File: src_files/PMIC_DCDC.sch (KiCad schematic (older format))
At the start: 49 parts

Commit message: littleupdate
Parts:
- C22, C23, C24, C25, C26, C27, C28, C29, C30, C31, C32, C33, C34, C35, C36, C37, C38, C39, C40, C41, C42, C43, C44, C45, C46, C47, C48, C49, C50, C51, C52, C53, C54, C55, C56, C57: renamed from C?; footprint (none) -> Capacitor_SMD:C_0402_1005Metric
- L1, L2, L3, L4, L5: renamed from L?; footprint (none) -> greencharge-footprints:SRP6540-5R6M
- R1, R2, R3, R4, R5, R6, R7: renamed from R?; footprint (none) -> Resistor_SMD:R_0402_1005Metric
- U2: renamed from U?; footprint (none) -> Package_DFN_QFN:TQFN-48-1EP_7x7mm_P0.5mm_EP5.1x5.1mm

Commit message: all screens added_3 items left
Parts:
- removed U2: RK809, Package_DFN_QFN:TQFN-48-1EP_7x7mm_P0.5mm_EP5.1x5.1mm, symbol GCL_Integrated-Circuits:RK809
- added U2: RK809, symbol GCL_Integrated-Circuits:RK809
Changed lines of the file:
@@
 $Descr A4 11693 8268
 encoding utf-8
-Sheet 3 11
+Sheet 3 12
 Title ""
 Date ""
@@
 Wire Wire Line
 	4875 1075 4550 1075
-$Comp
-L GCL_Integrated-Circuits:RK809 U?
-U 1 1 61D17743
-P 5875 925
-AR Path="/61D17743" Ref="U?"  Part="3"
-AR Path="/61CF51BC/61D17743" Ref="U2"  Part="1"
-F 0 "U2" H 5775 1075 50  0000 C CNN
-F 1 "RK809" H 5750 975 50  0000 C CNN
-F 2 "Package_DFN_QFN:TQFN-48-1EP_7x7mm_P0.5mm_EP5.1x5.1mm" H 5775 1125 50  0001 C CNN
-F 3 "" H 5775 1125 50  0001 C CNN
-	1    5875 925
-	1    0    0    -1
-$EndComp
 Text Label 3525 2275 0    50   ~ 0
 SW2
@@
 Wire Wire Line
 	6675 3825 6875 3825
+$Comp
+L GCL_Integrated-Circuits:RK809 U2
+U 3 1 625FB264
+P 5875 925
+F 0 "U2" H 5775 1090 50  0000 C CNN
+F 1 "RK809" H 5775 999 50  0000 C CNN
+F 2 "" H 5775 1125 50  0001 C CNN
+F 3 "" H 5775 1125 50  0001 C CNN
+	3    5875 925
+	1    0    0    -1
+$EndComp
 $EndSCHEMATC

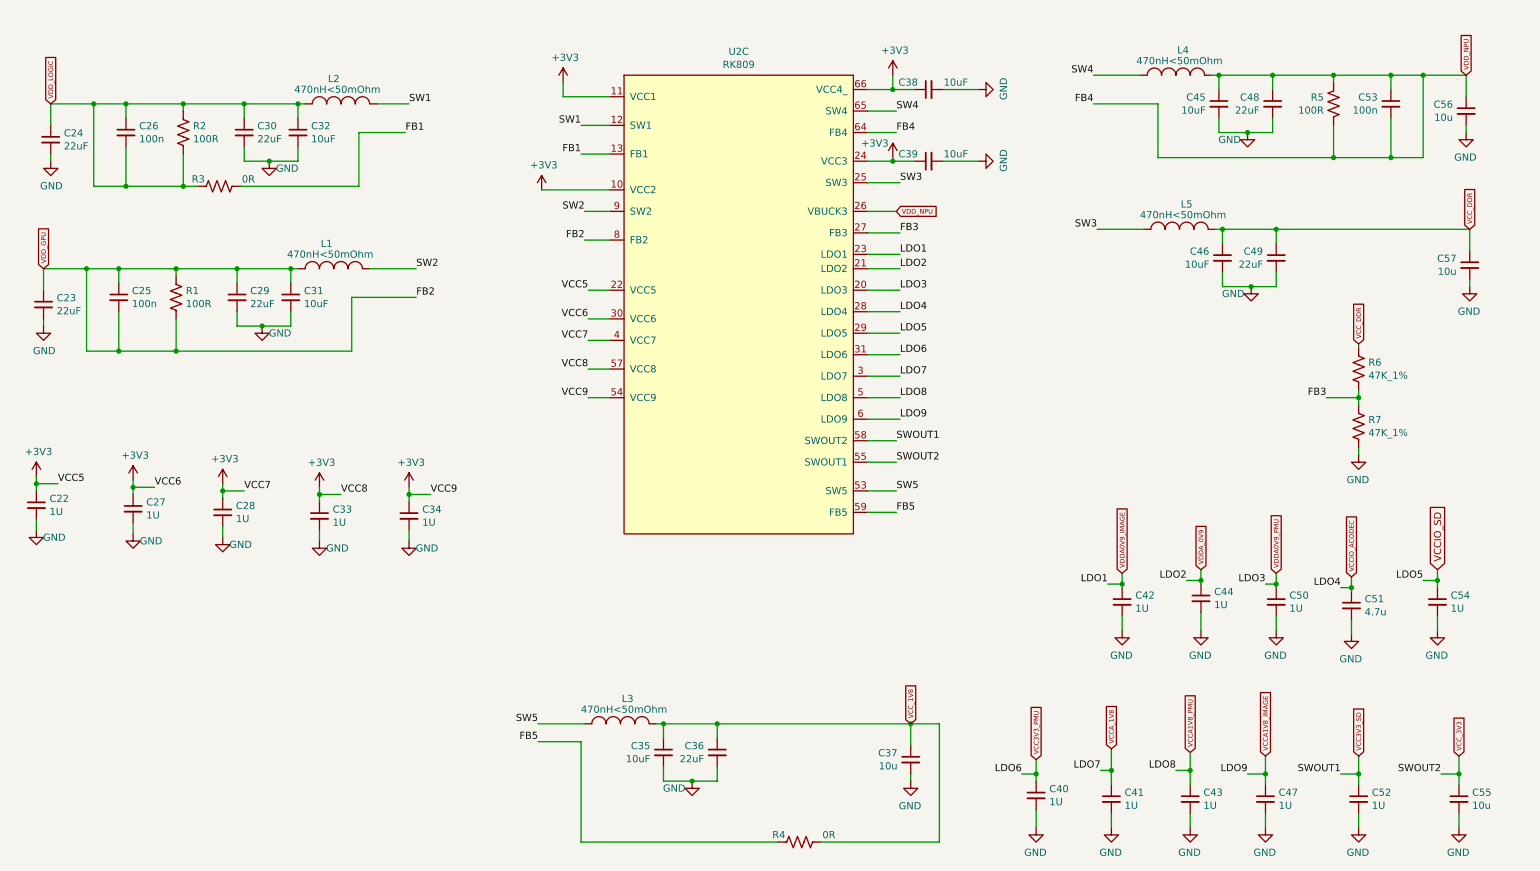
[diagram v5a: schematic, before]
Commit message: schematic capture complete
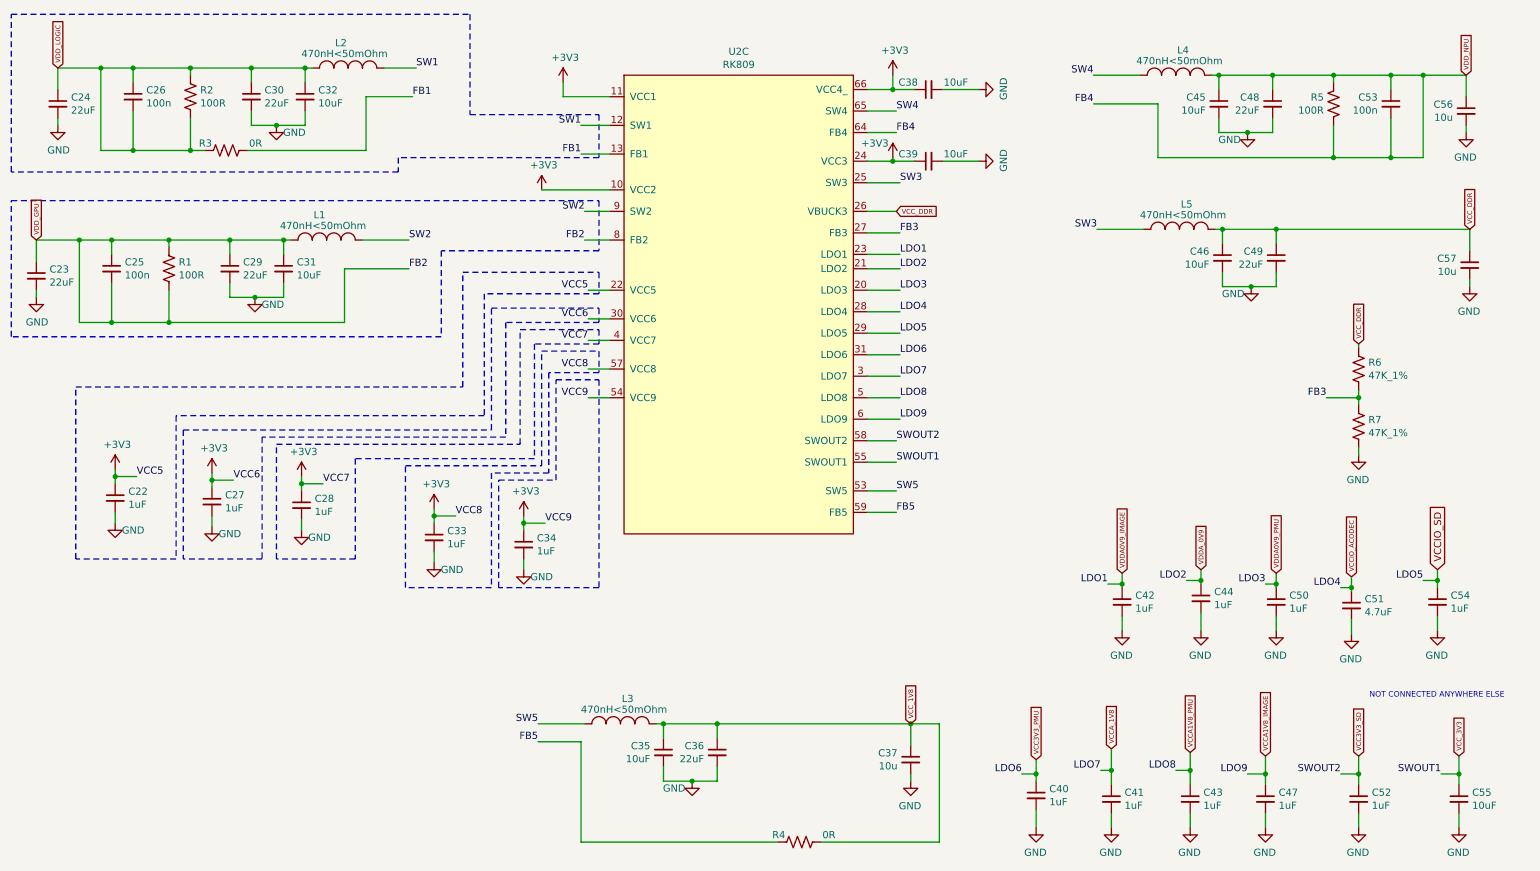
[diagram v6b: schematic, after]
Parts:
- C22, C27, C28, C33, C34, C40, C41, C42, C43, C44, C47, C50, C52, C54: value 1U -> 1uF
- C51: value 4.7u -> 4.7uF
- C55: value 10u -> 10uF
- L1, L2, L3, L4, L5: footprint greencharge-footprints:SRP6540-5R6M -> greencharge-footprints:252010CDMCDDS-R47MC
- U2: footprint (none) -> greencharge-footprints:QFN-68_EP_7x7_Pitch0.35mm
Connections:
- net VCC_DDR: now also U2.26 (VBUCK3)
- net VDD_NPU: no longer U2.26 (VBUCK3)
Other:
- note added: "NOT CONNECTED ANYWHERE ELSE"
- moved on the sheet: C22, C23, C24, C25, C26, C27, C28, C29, C30, C31, C32, C33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
